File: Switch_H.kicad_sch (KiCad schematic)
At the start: 11 parts, among them Q201 NVTFWS4D9N04XMTAG, Q202 NVTFWS4D9N04XMTAG, U201 LM74700, U202 LM74700

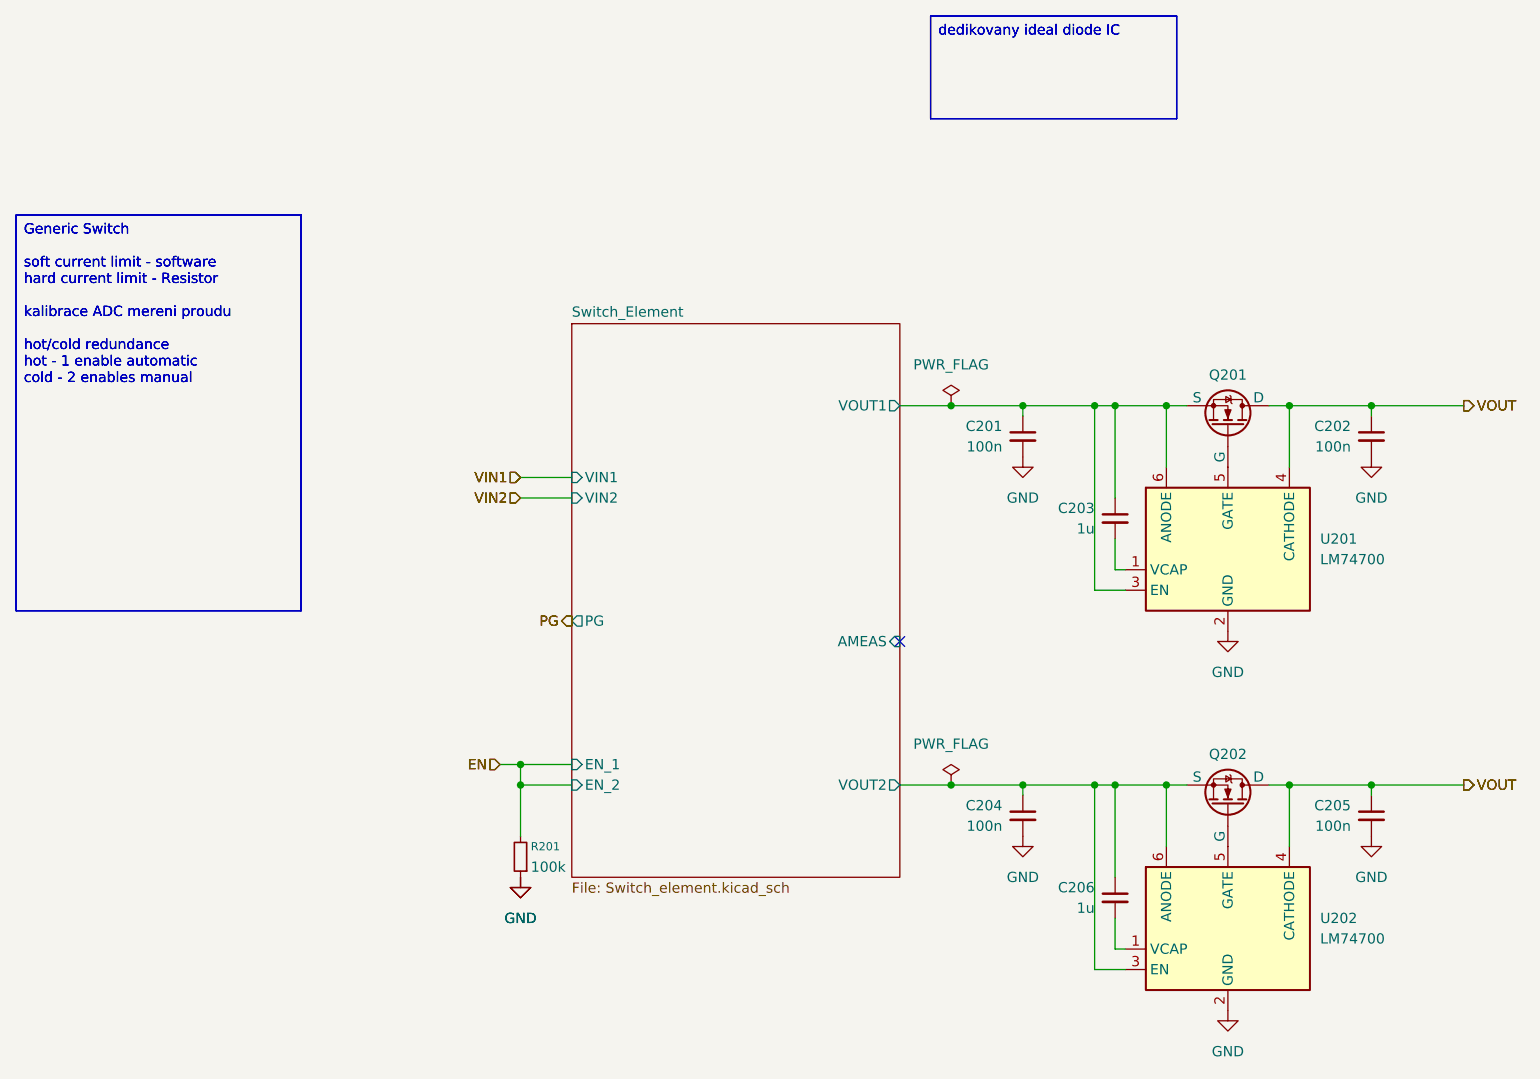
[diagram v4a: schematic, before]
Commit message: pcb progres for all components
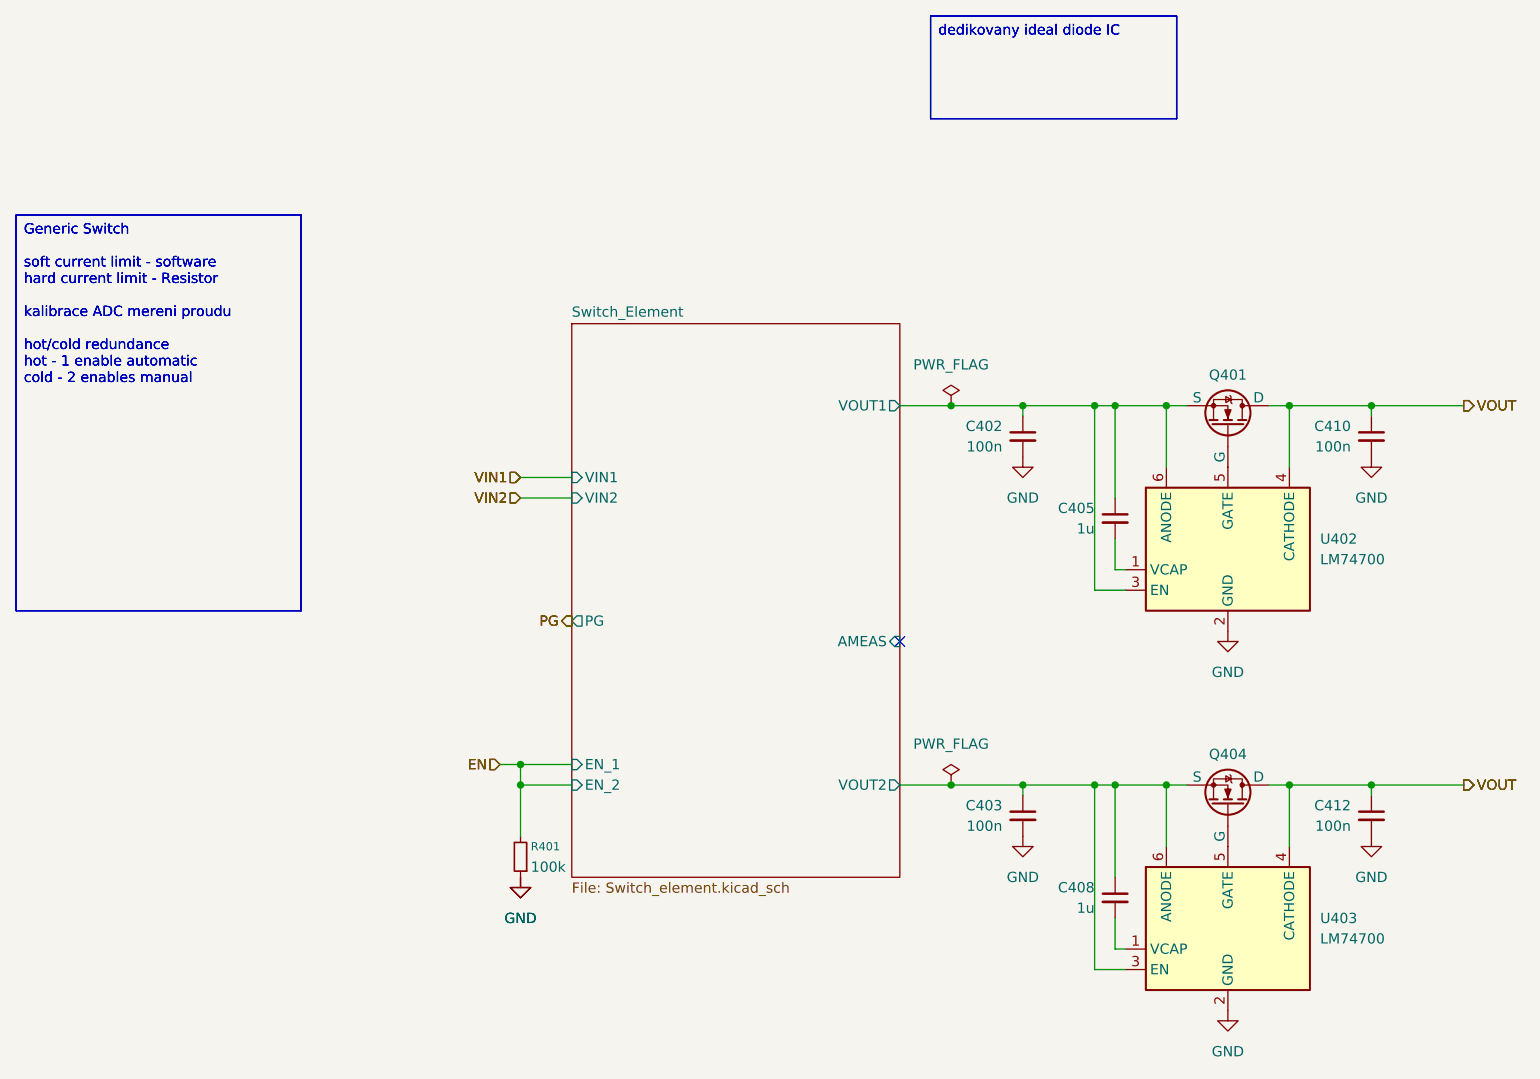
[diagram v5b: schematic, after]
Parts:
- renumbered C201 to C402, C204 to C403, C203 to C405, C206 to C408, C202 to C410, C205 to C412, Q201 to Q401, Q202 to Q404, R201 to R401, U201 to U402, U202 to U403

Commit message: progress on PCBs
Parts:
- renumbered C402 to C1301, C410 to C1302, C405 to C1303, C403 to C1304, C412 to C1305, C408 to C1306, Q401 to Q1301, Q404 to Q1302, R401 to R1301, U402 to U1301, U403 to U1302
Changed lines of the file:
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@@
 		(dnp no)
 		(fields_autoplaced yes)
-		(property "Reference" "#PWR0411"
+		(property "Reference" "#PWR01302"
 			(at 191.77 76.2 0)
 			(effects
@@
 		(dnp no)
 		(fields_autoplaced yes)
-		(property "Reference" "#FLG0402"
+		(property "Reference" "#FLG01302"
 			(at 139.7 108.585 0)
 			(effects
@@
 		(dnp no)
 		(fields_autoplaced yes)
-		(property "Reference" "#FLG0401"
+		(property "Reference" "#FLG01301"
 			(at 139.7 61.595 0)
 			(effects
@@
 		(on_board yes)
 		(dnp no)
-		(property "Reference" "R401"
+		(property "Reference" "R1301"
 			(at 87.63 118.11 0)
 			(effects
@@
 		(on_board yes)
 		(dnp no)
-		(property "Reference" "Q401"
+		(property "Reference" "Q1301"
 			(at 173.99 59.69 90)
 			(effects
@@
 		(dnp no)
 		(fields_autoplaced yes)
-		(property "Reference" "#PWR0401"
+		(property "Reference" "#PWR01306"
 			(at 86.36 128.27 0)
 			(effects
@@
 		(dnp no)
 		(fields_autoplaced yes)
-		(property "Reference" "#PWR0408"
+		(property "Reference" "#PWR01303"
 			(at 173.99 97.79 0)
 			(effects
@@
 		(dnp no)
 		(fields_autoplaced yes)
-		(property "Reference" "#PWR0409"
+		(property "Reference" "#PWR01308"
 			(at 173.99 144.78 0)
 			(effects
@@
 		(dnp no)
 		(fields_autoplaced yes)
-		(property "Reference" "#PWR0404"
+		(property "Reference" "#PWR01301"
 			(at 148.59 76.2 0)
 			(effects
@@
 		(dnp no)
 		(fields_autoplaced yes)
-		(property "Reference" "#PWR0414"
+		(property "Reference" "#PWR01305"
 			(at 191.77 123.19 0)
 			(effects
@@
 		(dnp no)
 		(fields_autoplaced yes)
-		(property "Reference" "U403"
+		(property "Reference" "U1302"
 			(at 185.42 126.9999 0)
 			(effects
@@
 		(on_board yes)
 		(dnp no)
-		(property "Reference" "C403"
+		(property "Reference" "C1304"
 			(at 146.05 113.0362 0)
 			(effects
@@
 		(on_board yes)
 		(dnp no)
-		(property "Reference" "C405"
+		(property "Reference" "C1303"
 			(at 157.48 76.2062 0)
 			(effects
@@
 		(on_board yes)
 		(dnp no)
-		(property "Reference" "C402"
+		(property "Reference" "C1301"
 			(at 146.05 66.0462 0)
 			(effects
@@
 		(on_board yes)
 		(dnp no)
-		(property "Reference" "C410"
+		(property "Reference" "C1302"
 			(at 189.23 66.0462 0)
 			(effects
@@
 		(dnp no)
 		(fields_autoplaced yes)
-		(property "Reference" "#PWR0405"
+		(property "Reference" "#PWR01304"
 			(at 148.59 123.19 0)
 			(effects
@@
 		(on_board yes)
 		(dnp no)
-		(property "Reference" "C412"
+		(property "Reference" "C1305"
 			(at 189.23 113.0362 0)
 			(effects
@@
 		(on_board yes)
 		(dnp no)
-		(property "Reference" "Q404"
+		(property "Reference" "Q1302"
 			(at 173.99 106.68 90)
 			(effects
@@
 		(dnp no)
 		(fields_autoplaced yes)
-		(property "Reference" "U402"
+		(property "Reference" "U1301"
 			(at 185.42 80.0099 0)
 			(effects
@@
 		(dnp no)
 		(fields_autoplaced yes)
-		(property "Reference" "#PWR0402"
+		(property "Reference" "#PWR01307"
 			(at 86.36 128.27 0)
 			(effects
@@
 		(on_board yes)
 		(dnp no)
-		(property "Reference" "C408"
+		(property "Reference" "C1306"
 			(at 157.48 123.1962 0)
 			(effects
